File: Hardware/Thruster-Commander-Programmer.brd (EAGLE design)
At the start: 38.1 x 21.6 mm, 12 parts, among them J1 AVR_SPI_PROG_3X2PTH

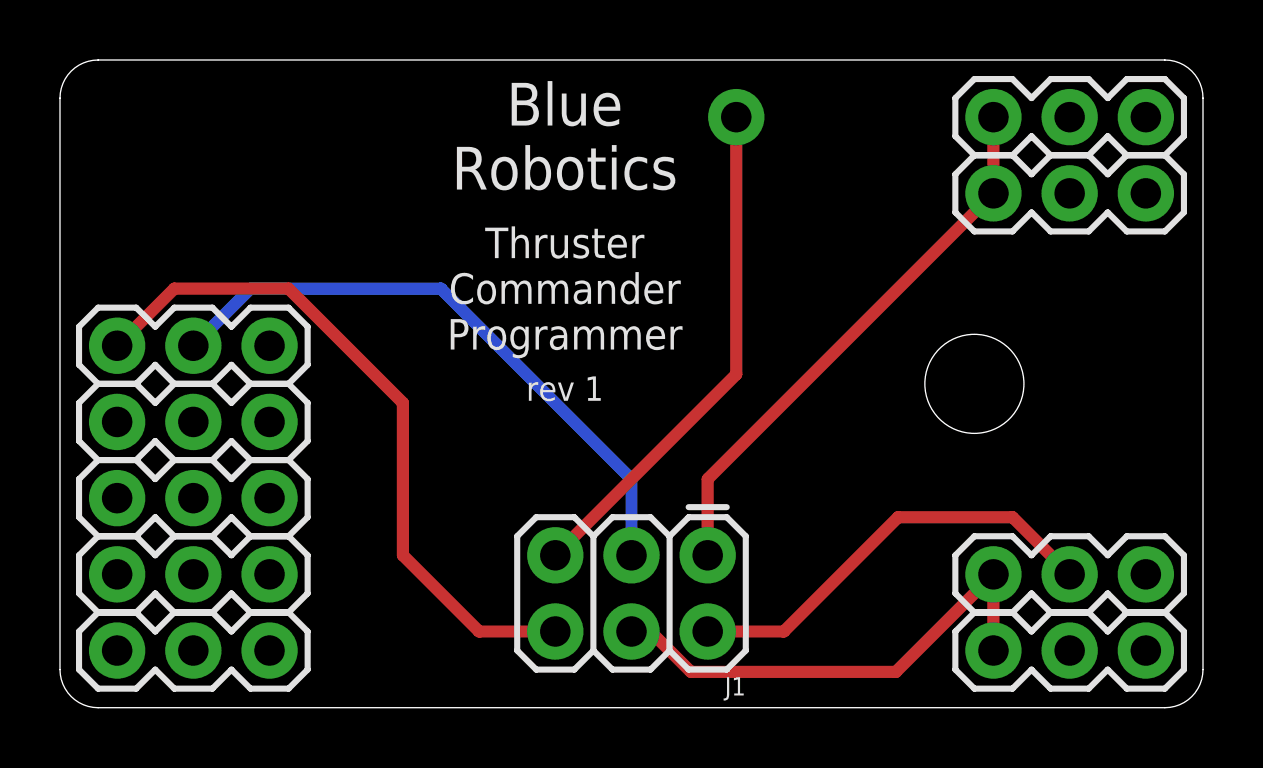
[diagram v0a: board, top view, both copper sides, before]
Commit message: Fix programmer board MISO/MOSI connections
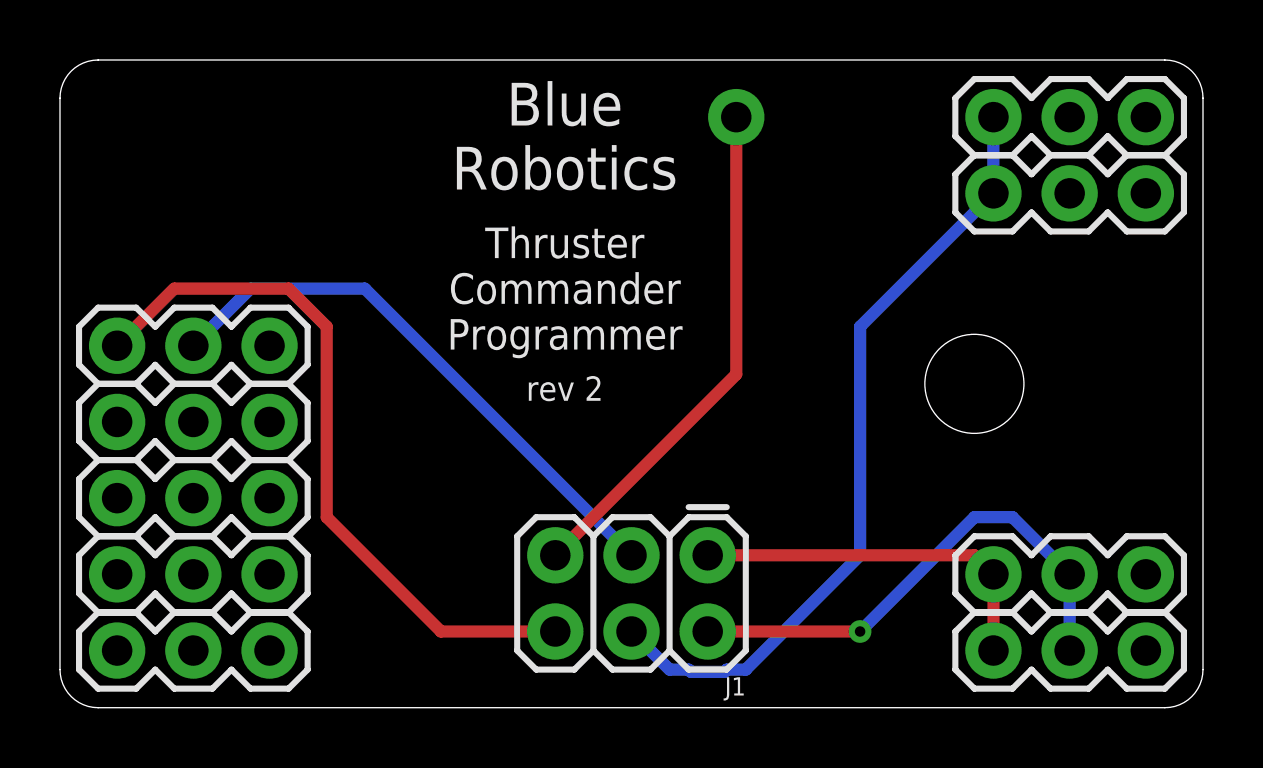
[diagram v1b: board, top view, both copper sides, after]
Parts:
- renumbered PWM0A to PWM_L_A, PWM0B to PWM_L_B, PWM1A to PWM_R_A, PWM1B to PWM_R_B
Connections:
- removed net PWM0: J1.4, PWM_L_A.1, PWM_L_B.1
- removed net PWM1: J1.1, PWM_R_A.1, PWM_R_B.1
- new net PWM_L: J1.1, PWM_L_A.1, PWM_L_B.1
- new net PWM_R: J1.4, PWM_R_A.1, PWM_R_B.1
- net +5V: now also PWM_L_B.2
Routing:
- net PWM_R: track 0.00 -> 26.2 mm
- net PWM1: track 18.6 -> 0.00 mm
- net PWM0: track 16.5 -> 0.00 mm
- net PWM_L: track 0.00 -> 12.3 mm
- net +5V: track 14.4 -> 17.0 mm, vias 0 -> 1
- net SWITCH: track 20.6 -> 19.1 mm
- net GND: track 23.1 -> 23.8 mm
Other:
- board text added: "rev 2"
- board text removed: "rev 1"
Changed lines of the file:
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@@
 <text x="16.8275" y="19.05" size="1.4224" layer="21" ratio="12" align="center">Blue
 Robotics</text>
-<text x="16.8275" y="10.63625" size="0.8128" layer="21" ratio="12" align="center">rev 1</text>
+<text x="16.8275" y="10.63625" size="0.8128" layer="21" ratio="12" align="center">rev 2</text>
 </plain>
 <attributes>
@@
 <attribute name="VALUE" x="0.635" y="3.81" size="1.27" layer="27"/>
 </element>
-<element name="PWM0A" library="SparkFun-Connectors" package="1X03" value="" x="31.115" y="4.445" smashed="yes">
+<element name="PWM_L_A" library="SparkFun-Connectors" package="1X03" value="" x="31.115" y="4.445" smashed="yes">
 <attribute name="VALUE" x="29.845" y="1.27" size="1.27" layer="27"/>
 </element>
-<element name="PWM0B" library="SparkFun-Connectors" package="1X03" value="" x="31.115" y="1.905" smashed="yes">
+<element name="PWM_L_B" library="SparkFun-Connectors" package="1X03" value="" x="31.115" y="1.905" smashed="yes">
 <attribute name="VALUE" x="29.845" y="-1.27" size="1.27" layer="27"/>
 </element>
-<element name="PWM1A" library="SparkFun-Connectors" package="1X03" value="" x="31.115" y="17.145" smashed="yes">
+<element name="PWM_R_A" library="SparkFun-Connectors" package="1X03" value="" x="31.115" y="17.145" smashed="yes">
 <attribute name="VALUE" x="29.845" y="13.97" size="1.27" layer="27"/>
 </element>
-<element name="PWM1B" library="SparkFun-Connectors" package="1X03" value="" x="31.115" y="19.685" smashed="yes">
+<element name="PWM_R_B" library="SparkFun-Connectors" package="1X03" value="" x="31.115" y="19.685" smashed="yes">
 <attribute name="VALUE" x="29.845" y="16.51" size="1.27" layer="27"/>
 </element>
@@
 <contactref element="SW" pad="1"/>
 <contactref element="J1" pad="6"/>
-<wire x1="16.51" y1="2.54" x2="13.97" y2="2.54" width="0.4064" layer="1"/>
-<wire x1="13.97" y1="2.54" x2="11.43" y2="5.08" width="0.4064" layer="1"/>
-<wire x1="11.43" y1="5.08" x2="11.43" y2="10.16" width="0.4064" layer="1"/>
-<wire x1="11.43" y1="10.16" x2="7.62" y2="13.97" width="0.4064" layer="1"/>
+<wire x1="1.905" y1="12.065" x2="3.81" y2="13.97" width="0.4064" layer="1"/>
 <wire x1="7.62" y1="13.97" x2="3.81" y2="13.97" width="0.4064" layer="1"/>
-<wire x1="3.81" y1="13.97" x2="1.905" y2="12.065" width="0.4064" layer="1"/>
+<wire x1="7.62" y1="13.97" x2="8.89" y2="12.7" width="0.4064" layer="1"/>
+<wire x1="8.89" y1="12.7" x2="8.89" y2="6.35" width="0.4064" layer="1"/>
+<wire x1="8.89" y1="6.35" x2="12.7" y2="2.54" width="0.4064" layer="1"/>
+<wire x1="12.7" y1="2.54" x2="16.51" y2="2.54" width="0.4064" layer="1"/>
 </signal>
 <signal name="+5V">
 <contactref element="J1" pad="2"/>
-<contactref element="PWM0A" pad="2"/>
-<wire x1="21.59" y1="2.54" x2="24.13" y2="2.54" width="0.4064" layer="1"/>
-<wire x1="24.13" y1="2.54" x2="27.94" y2="6.35" width="0.4064" layer="1"/>
-<wire x1="27.94" y1="6.35" x2="31.75" y2="6.35" width="0.4064" layer="1"/>
-<wire x1="31.75" y1="6.35" x2="33.655" y2="4.445" width="0.4064" layer="1"/>
+<contactref element="PWM_L_A" pad="2"/>
+<contactref element="PWM_L_B" pad="2"/>
+<wire x1="21.59" y1="2.54" x2="26.67" y2="2.54" width="0.4064" layer="1"/>
+<via x="26.67" y="2.54" extent="1-16" drill="0.35"/>
+<wire x1="26.67" y1="2.54" x2="30.48" y2="6.35" width="0.4064" layer="16"/>
+<wire x1="30.48" y1="6.35" x2="31.75" y2="6.35" width="0.4064" layer="16"/>
+<wire x1="31.75" y1="6.35" x2="33.655" y2="4.445" width="0.4064" layer="16"/>
+<wire x1="33.655" y1="4.445" x2="33.655" y2="1.905" width="0.4064" layer="16"/>
 </signal>
 <signal name="RESET">
 <contactref element="JP2" pad="1"/>
 <contactref element="J1" pad="5"/>
-<wire x1="22.5425" y1="19.685" x2="22.5425" y2="11.1125" width="0.4064" layer="1"/>
-<wire x1="22.5425" y1="11.1125" x2="16.51" y2="5.08" width="0.4064" layer="1"/>
+<wire x1="16.51" y1="5.08" x2="22.5425" y2="11.1125" width="0.4064" layer="1"/>
+<wire x1="22.5425" y1="11.1125" x2="22.5425" y2="19.685" width="0.4064" layer="1"/>
 </signal>
 <signal name="THROTTLE1">
@@
 <signal name="THROTTLE0">
 <contactref element="THR0" pad="2"/>
-</signal>
-<signal name="PWM0">
-<contactref element="PWM0A" pad="1"/>
-<contactref element="PWM0B" pad="1"/>
-<contactref element="J1" pad="4"/>
-<wire x1="19.05" y1="2.54" x2="19.68618125" y2="2.54" width="0.4064" layer="1"/>
-<wire x1="19.68618125" y1="2.54" x2="21.03238125" y2="1.1938" width="0.4064" layer="1"/>
-<wire x1="21.03238125" y1="1.1938" x2="27.8638" y2="1.1938" width="0.4064" layer="1"/>
-<wire x1="27.8638" y1="1.1938" x2="31.115" y2="4.445" width="0.4064" layer="1"/>
-<wire x1="31.115" y1="4.445" x2="31.115" y2="1.905" width="0.4064" layer="1"/>
-</signal>
-<signal name="PWM1">
-<contactref element="PWM1A" pad="1"/>
-<contactref element="PWM1B" pad="1"/>
-<contactref element="J1" pad="1"/>
-<wire x1="21.59" y1="5.08" x2="21.59" y2="7.62" width="0.4064" layer="1"/>
-<wire x1="21.59" y1="7.62" x2="31.115" y2="17.145" width="0.4064" layer="1"/>
-<wire x1="31.115" y1="17.145" x2="31.115" y2="19.685" width="0.4064" layer="1"/>
 </signal>
 <signal name="STEERING">
@@
 <contactref element="SW" pad="2"/>
 <contactref element="J1" pad="3"/>
-<wire x1="19.05" y1="5.08" x2="19.05" y2="7.62" width="0.4064" layer="16"/>
-<wire x1="19.05" y1="7.62" x2="12.7" y2="13.97" width="0.4064" layer="16"/>
-<wire x1="12.7" y1="13.97" x2="6.35" y2="13.97" width="0.4064" layer="16"/>
+<wire x1="19.05" y1="5.08" x2="10.16" y2="13.97" width="0.4064" layer="16"/>
+<wire x1="10.16" y1="13.97" x2="6.35" y2="13.97" width="0.4064" layer="16"/>
 <wire x1="6.35" y1="13.97" x2="4.445" y2="12.065" width="0.4064" layer="16"/>
 </signal>
+<signal name="PWM_L">
+<contactref element="PWM_L_A" pad="1"/>
+<contactref element="PWM_L_B" pad="1"/>
+<contactref element="J1" pad="1"/>
+<wire x1="21.59" y1="5.08" x2="30.48" y2="5.08" width="0.4064" layer="1"/>
+<wire x1="31.115" y1="4.445" x2="30.48" y2="5.08" width="0.4064" layer="1"/>
+<wire x1="31.115" y1="1.905" x2="31.115" y2="4.445" width="0.4064" layer="1"/>
+</signal>
+<signal name="PWM_R">
+<contactref element="PWM_R_A" pad="1"/>
+<contactref element="PWM_R_B" pad="1"/>
+<contactref element="J1" pad="4"/>
+<wire x1="31.115" y1="17.145" x2="31.115" y2="19.685" width="0.4064" layer="16"/>
+<wire x1="19.05" y1="2.54" x2="20.32" y2="1.27" width="0.4064" layer="16"/>
+<wire x1="20.32" y1="1.27" x2="20.95618125" y2="1.27" width="0.4064" layer="16"/>
+<wire x1="20.95618125" y1="1.27" x2="21.03238125" y2="1.1938" width="0.4064" layer="16"/>
+<wire x1="21.03238125" y1="1.1938" x2="22.14761875" y2="1.1938" width="0.4064" layer="16"/>
+<wire x1="22.14761875" y1="1.1938" x2="22.22381875" y2="1.27" width="0.4064" layer="16"/>
+<wire x1="22.22381875" y1="1.27" x2="22.86" y2="1.27" width="0.4064" layer="16"/>
+<wire x1="22.86" y1="1.27" x2="26.67" y2="5.08" width="0.4064" layer="16"/>
+<wire x1="26.67" y1="5.08" x2="26.67" y2="12.7" width="0.4064" layer="16"/>
+<wire x1="26.67" y1="12.7" x2="31.115" y2="17.145" width="0.4064" layer="16"/>
+</signal>
 </signals>
